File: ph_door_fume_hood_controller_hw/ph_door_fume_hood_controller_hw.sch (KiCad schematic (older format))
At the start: 249 parts, among them IC1 6N137, IC2 6N137, J1 Conn_01x03, J10 Conn_01x03, J11 Conn_01x02, J12 Conn_01x06, J13 Conn_01x02, J14 Conn_01x03, J15 Conn_01x03, J2 Conn_01x04, J3 CONN_01X04, J4 Conn_01x03, J5 Conn_01x03, J6 Conn_01x02, J7 Conn_01x06, J8 USB_OTG, J9 Conn_01x02, M1 DC-DC-24-12V-200mA, M2 MORSUN_485, Q1 C1815, Q10 A1015, Q11 Q_NMOS_GDS, Q2 Q_PMOS_GDS, Q3 Q_NMOS_GDS, Q4 Q_NMOS_GDS, Q5 C1815, Q6 Q_NMOS_GDS, Q7 Q_NMOS_GDS, Q8 C1815, Q9 Q_NMOS_GDS, U1 74HC123, U10 PC817, U11 MCP4725, U12 ASM1117-3V3, U13 PC817, U14 PC817, U15 LM358, U16 PC817, U17 PC817, U18 PC817, U19 PC817, U2 AD8601, U20 PC817, U21 PC817, U22 PC817, U23 PC817, U3 PC817, U4 PC817, U5 TB6600, U6 PC817, U7 STM32F103C8, U8 ASM1117, U9 XL4015, Y1 Crystal, Y2 32768Mhz

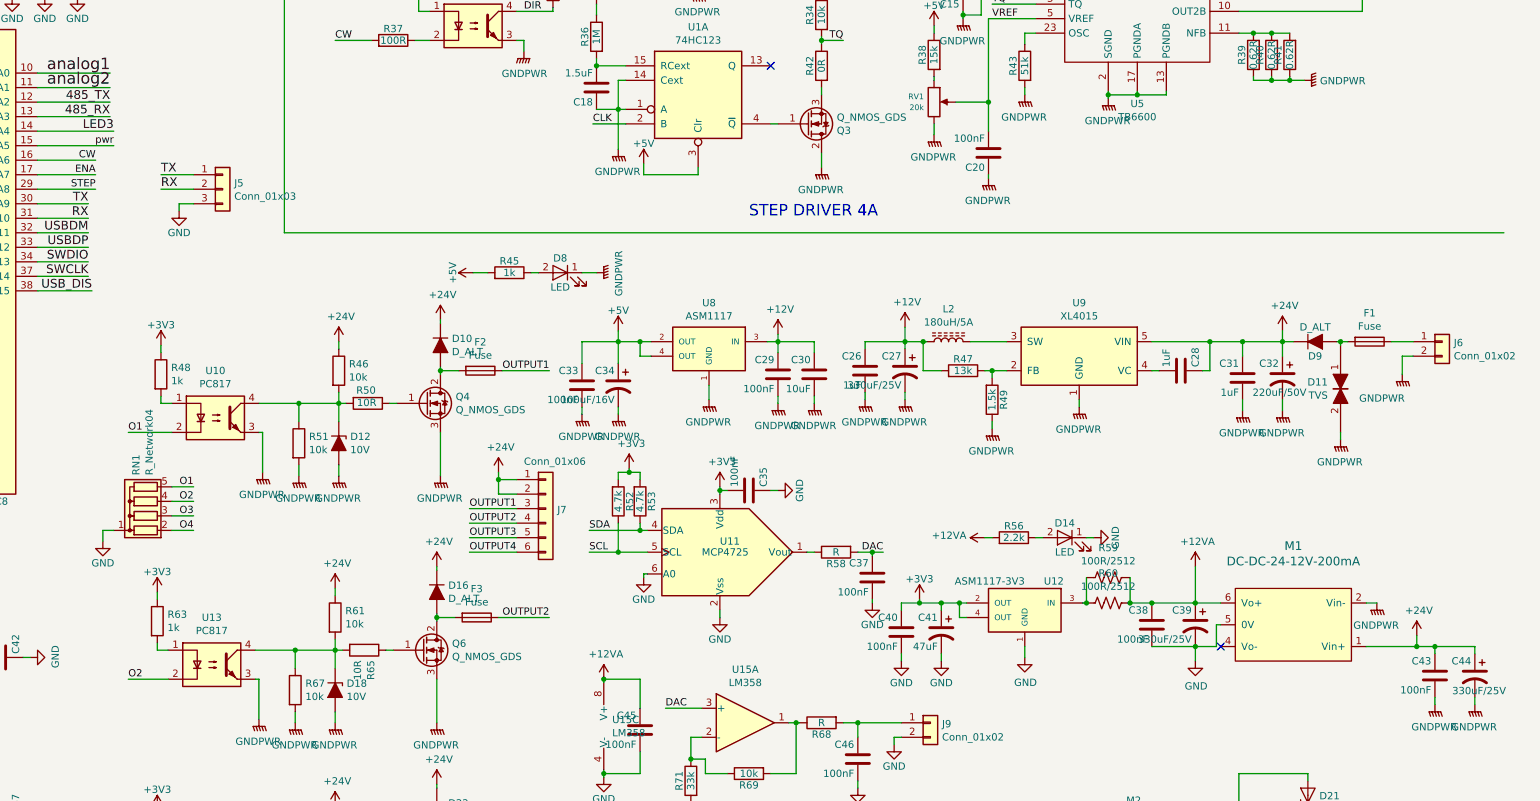
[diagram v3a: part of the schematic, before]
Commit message: door_fume_hood
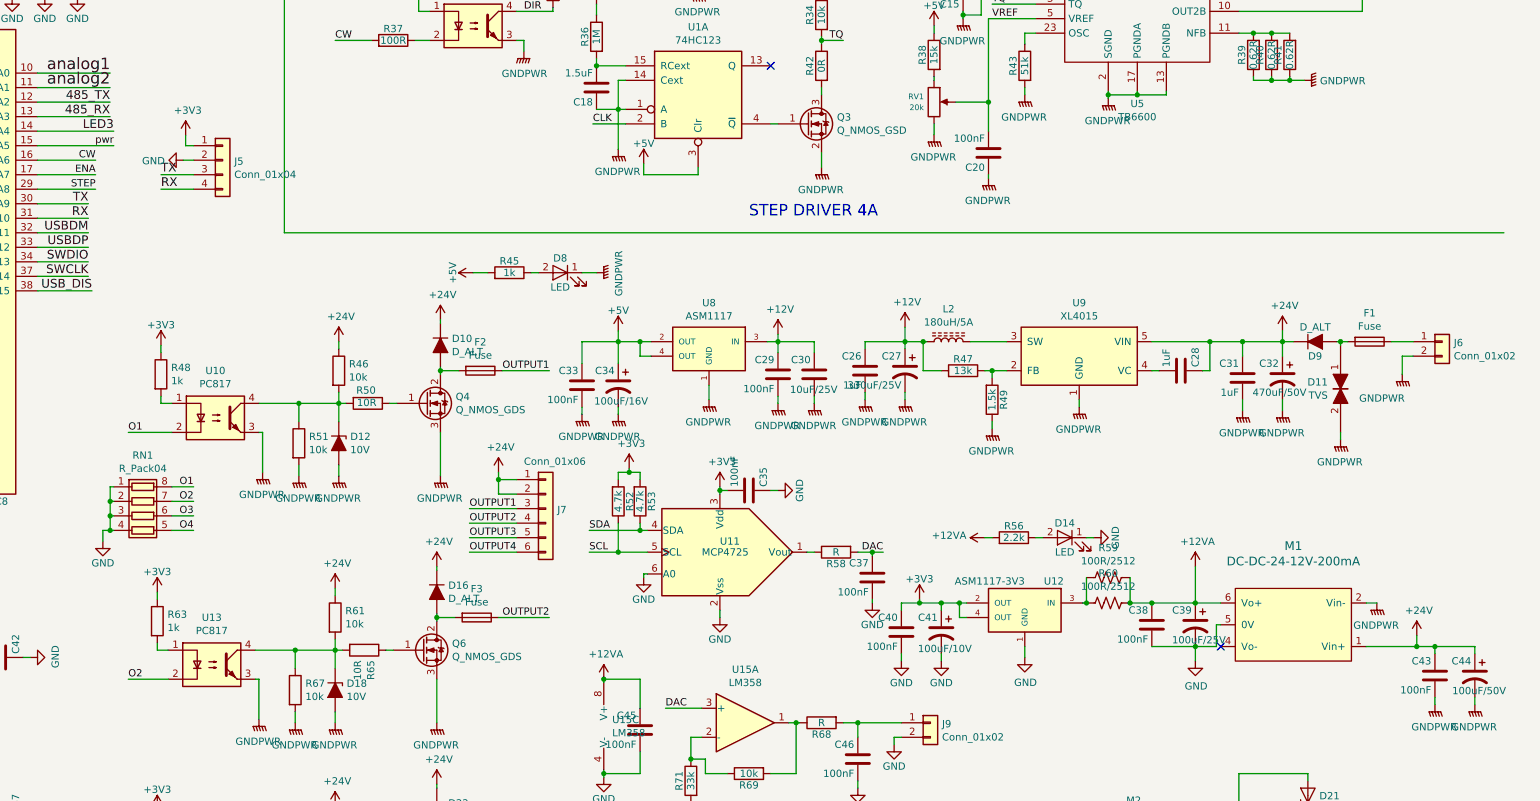
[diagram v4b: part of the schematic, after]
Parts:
- removed J5: Conn_01x03, Connector_PinSocket_2.54mm:PinSocket_1x03_P2.54mm_Vertical, symbol Connector_Generic:Conn_01x03
- removed Q3: Q_NMOS_GDS, VinhTho_Lib:TO-252-2, symbol Device:Q_NMOS_GDS
- removed RN1: R_Network04, Resistor_THT:R_Array_SIP5, symbol Device:R_Network04
- added J5: Conn_01x04, Connector_PinHeader_2.54mm:PinHeader_1x04_P2.54mm_Vertical, symbol Connector_Generic:Conn_01x04
- added Q3: Q_NMOS_GSD, VinhTho_Lib:SOT-23, symbol mcu_water_sample_hw-rescue:Q_NMOS_GSD
- added RN1: R_Pack04, Resistor_SMD:R_Array_Convex_4x0603, symbol Device:R_Pack04
- C27: footprint Capacitor_SMD:C_1210_3225Metric_Pad1.42x2.65mm_HandSolder -> Capacitor_SMD:CP_Elec_8x10.5
- C30: value 10uF -> 10uF/25V; footprint Capacitor_SMD:C_0805_2012Metric_Pad1.15x1.40mm_HandSolder -> Capacitor_SMD:C_1210_3225Metric_Pad1.42x2.65mm_HandSolder
- C32: value 220uF/50V -> 470uF/50V; footprint Capacitor_SMD:C_1210_3225Metric_Pad1.42x2.65mm_HandSolder -> Capacitor_SMD:CP_Elec_10x14.3
- C34: footprint Capacitor_SMD:C_1210_3225Metric_Pad1.42x2.65mm_HandSolder -> Capacitor_SMD:CP_Elec_6.3x5.4
- C39: value 330uF/25V -> 100uF/25V; footprint Capacitor_SMD:C_1210_3225Metric_Pad1.42x2.65mm_HandSolder -> Capacitor_Tantalum_SMD:CP_EIA-7343-20_Kemet-V_Pad2.25x2.55mm_HandSolder
- C41: value 47uF -> 100uF/10V; footprint Capacitor_SMD:C_1210_3225Metric_Pad1.42x2.65mm_HandSolder -> Capacitor_Tantalum_SMD:CP_EIA-3528-15_AVX-H_Pad1.50x2.35mm_HandSolder
- C44: value 330uF/25V -> 100uF/50V; footprint Capacitor_SMD:C_1210_3225Metric_Pad1.42x2.65mm_HandSolder -> Capacitor_Tantalum_SMD:CP_EIA-7343-31_Kemet-D_Pad2.25x2.55mm_HandSolder
- F1: footprint VinhTho_Lib:Fuse_SMD1812 -> VinhTho_Lib:Fuseholder5x20_horiz_SemiClosed_Casing10x25mm
- J11: footprint VinhTho_Lib:TerminalBlock_WAGO-236_2Stift_R5mm_2pol -> VinhTho_Lib:TerminalBlock_WAGO_2.54mm_2P
- J12: footprint VinhTho_Lib:TerminalBlock-WAGO-6P -> VinhTho_Lib:TerminalBlock_WAGO_2.54mm_6P
- J2: footprint VinhTho_Lib:Domino-5.08mm_4pol -> VinhTho_Lib:TerminalBlock_WAGO-236_2Stift_R5mm_4pol
- L2: footprint VinhTho_Lib:L181-5A -> VinhTho_Lib:Inductor_5A
- RV1: footprint VinhTho_Lib:VR1 -> VinhTho_Lib:VR-3362P
- U10, U13, U14, U16, U17, U18, U19, U20, U21, U22, U23, U3, U4, U6: footprint Package_DIP:DIP-4_W7.62mm -> VinhTho_Lib:Optocoupler_SMD
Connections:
- net +3V3: now also J5.1 (Pin_1)
- net GND: now also J5.2 (Pin_2), RN1.1 (R1.1), RN1.2 (R2.1), RN1.3 (R3.1), RN1.4 (R4.1)
- net GNDPWR: now also Q3.2 (S)
- net O1: now also RN1.8 (R1.2)
- net O2: now also RN1.7 (R2.2)
- net O3: now also RN1.6 (R3.2)
- net O4: now also RN1.5 (R4.2)
- net RX: now also J5.4 (Pin_4)
- net TX: now also J5.3 (Pin_3)
- net at U1.4 (~Q): now also Q3.1 (G)
- net at R42.2: now also Q3.3 (D)

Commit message: Layoutting door fume
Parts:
- removed Q11, Q4, Q6, Q7, Q9: Q_NMOS_GDS, VinhTho_Lib:TO-252-2, symbol Device:Q_NMOS_GDS
- removed R25, R5: 0R, Resistor_SMD:R_0805_2012Metric_Pad1.15x1.40mm_HandSolder, symbol Device:R
- added Q11, Q4, Q6, Q7, Q9: Q_NMOS_GSD, VinhTho_Lib:SOT-23, symbol Device:Q_NMOS_GSD
- J13: footprint VinhTho_Lib:TerminalBlock_WAGO-236_2Stift_R5mm_2pol -> VinhTho_Lib:TerminalBlock_WAGO_2.54mm_2P
- J7: footprint VinhTho_Lib:TerminalBlock-WAGO-6P -> VinhTho_Lib:TerminalBlock_WAGO_2.54mm_6P
- J9: footprint VinhTho_Lib:TerminalBlock_WAGO-236_2Stift_R5mm_2pol -> Connector_PinSocket_2.54mm:PinSocket_1x02_P2.54mm_Vertical
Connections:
- net +3V3: now also D15.1 (K), LS1.1
- net +5V: no longer C36.1, D13.1 (K), D15.1 (K), LS1.1
- net GNDPWR: now also Q11.2 (S), Q4.2 (S), Q6.2 (S), Q7.2 (S), Q9.2 (S)
- net at R50.1: now also Q4.1 (G)
- net at D10.2 (A), F2.2: now also Q4.3 (D)
- net at R65.1: now also Q6.1 (G)
- net at D16.2 (A), F3.2: now also Q6.3 (D)
- net at R77.1: now also Q7.1 (G)
- net at D22.2 (A), F4.2: now also Q7.3 (D)
- net at R93.1: now also Q11.1 (G)
- net at D30.2 (A), F7.2: now also Q11.3 (D)
- net at R87.1: now also Q9.1 (G)
- net at D26.2 (A), J13.2 (Pin_2): now also Q9.3 (D)
- new net +5VA: C36.1, D13.1 (K)
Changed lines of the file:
@@
 $EndComp
 $Comp
-L master-node-rescue:+5V #PWR0108
-U 1 1 5A52FEE6
-P 1700 5875
-F 0 "#PWR0108" H 1700 5725 50  0001 C CNN
-F 1 "+5V" H 1700 6015 50  0000 C CNN
-F 2 "" H 1700 5875 50  0001 C CNN
-F 3 "" H 1700 5875 50  0001 C CNN
-	1    1700 5875
-	1    0    0    -1
-$EndComp
-$Comp
-L master-node-rescue:D_ALT D13
-U 1 1 5A531888
-P 1450 5925
-F 0 "D13" H 1450 6025 50  0000 C CNN
-F 1 "D_ALT" H 1450 5825 50  0000 C CNN
-F 2 "VinhTho_Lib:D_SOD-323F" H 1450 5925 50  0001 C CNN
-F 3 "" H 1450 5925 50  0001 C CNN
-	1    1450 5925
-	-1   0    0    1
-$EndComp
-$Comp
 L master-node-rescue:R R55
 U 1 1 5A533DDA
@@
 $EndComp
 $Comp
-L master-node-rescue:+5V #PWR0116
-U 1 1 5A549BE9
-P 525 6050
-F 0 "#PWR0116" H 525 5900 50  0001 C CNN
-F 1 "+5V" H 525 6190 50  0000 C CNN
-F 2 "" H 525 6050 50  0001 C CNN
-F 3 "" H 525 6050 50  0001 C CNN
-	1    525  6050
-	1    0    0    -1
-$EndComp
-$Comp
 L master-node-rescue:CONN_01X04 J3
 U 1 1 5A54E099
@@
 	2950 5025 2600 5025
 Wire Wire Line
-	1300 5925 1300 6125
-Wire Wire Line
 	1300 6325 1350 6325
 Wire Wire Line
@@
 	2525 6600 2700 6600
 $Comp
-L master-node-rescue:+5V #PWR0121
-U 1 1 5F75627A
-P 2750 6375
-F 0 "#PWR0121" H 2750 6225 50  0001 C CNN
-F 1 "+5V" H 2750 6515 50  0000 C CNN
-F 2 "" H 2750 6375 50  0001 C CNN
-F 3 "" H 2750 6375 50  0001 C CNN
-	1    2750 6375
-	1    0    0    -1
-$EndComp
-Wire Wire Line
-	2750 6375 2750 6425
-$Comp
 L ph_door_fume_hood_controller_hw-rescue:C1815-nhantt-kicad-lib Q5
 U 1 1 5F78DF98
@@
 	1    0    0    -1
 $EndComp
-Wire Wire Line
-	1400 1725 1400 1700
 $Comp
 L power:GND #PWR034
@@
 in4
 $Comp
-L Device:R R25
-U 1 1 5DBE6FC7
-P 1125 1700
-F 0 "R25" H 1195 1746 50  0000 L CNN
-F 1 "0R" H 1195 1655 50  0000 L CNN
-F 2 "Resistor_SMD:R_0805_2012Metric_Pad1.15x1.40mm_HandSolder" V 1055 1700 50  0001 C CNN
-F 3 "~" H 1125 1700 50  0001 C CNN
-	1    1125 1700
-	0    1    1    0
-$EndComp
-Wire Wire Line
-	1275 1700 1400 1700
-Connection ~ 1400 1700
-Wire Wire Line
-	1400 1700 1400 1650
-$Comp
-L power:GNDPWR #PWR035
-U 1 1 5DC90838
-P 875 1750
-F 0 "#PWR035" H 875 1550 50  0001 C CNN
-F 1 "GNDPWR" H 880 1596 50  0000 C CNN
-F 2 "" H 875 1700 50  0001 C CNN
-F 3 "" H 875 1700 50  0001 C CNN
-	1    875  1750
-	-1   0    0    -1
-$EndComp
-Wire Wire Line
-	875  1750 875  1700
-Wire Wire Line
-	875  1700 975  1700
-$Comp
 L Device:R R4
 U 1 1 5DD3B3C6
@@
 	-1   0    0    1
 $EndComp
-$Comp
-L Device:R R5
-U 1 1 5DD3B78D
-P 1375 900
-F 0 "R5" H 1445 946 50  0000 L CNN
-F 1 "0R" H 1445 855 50  0000 L CNN
-F 2 "Resistor_SMD:R_0805_2012Metric_Pad1.15x1.40mm_HandSolder" V 1305 900 50  0001 C CNN
-F 3 "~" H 1375 900 50  0001 C CNN
-	1    1375 900
-	-1   0    0    1
-$EndComp
-Wire Wire Line
-	1100 1050 1375 1050
 Wire Wire Line
 	975  1050 1100 1050
-Connection ~ 1100 1050
 Wire Wire Line
 	1100 700  1100 750
@@
 	2125 2675 2075 2675
 $Comp
-L Device:Q_NMOS_GDS Q4
-U 1 1 5E6FB3F9
-P 8625 5400
-F 0 "Q4" H 8830 5446 50  0000 L CNN
-F 1 "Q_NMOS_GDS" H 8830 5355 50  0000 L CNN
-F 2 "VinhTho_Lib:TO-252-2" H 8825 5500 50  0001 C CNN
-F 3 "https://banlinhkien.com/30n06-fqd30n06-to252-mosfet-nch-22a-60v-p12118703.html" H 8625 5400 50  0001 C CNN
-	1    8625 5400
-	1    0    0    -1
-$EndComp
-$Comp
 L Device:R R50
 U 1 1 5E6FB731
@@
 	6800 5000 6800 5050
 $Comp
-L Device:Q_NMOS_GDS Q6
-U 1 1 5EF4FCDE
-P 8600 7100
-F 0 "Q6" H 8805 7146 50  0000 L CNN
-F 1 "Q_NMOS_GDS" H 8805 7055 50  0000 L CNN
-F 2 "VinhTho_Lib:TO-252-2" H 8800 7200 50  0001 C CNN
-F 3 "https://banlinhkien.com/30n06-fqd30n06-to252-mosfet-nch-22a-60v-p12118703.html" H 8600 7100 50  0001 C CNN
-	1    8600 7100
-	1    0    0    -1
-$EndComp
-$Comp
 L Device:R R65
 U 1 1 5EF4FCE4
@@
 $EndComp
 $Comp
-L Device:Q_NMOS_GDS Q7
-U 1 1 5F2858BF
-P 8600 8600
-F 0 "Q7" H 8805 8646 50  0000 L CNN
-F 1 "Q_NMOS_GDS" H 8805 8555 50  0000 L CNN
-F 2 "VinhTho_Lib:TO-252-2" H 8800 8700 50  0001 C CNN
-F 3 "https://banlinhkien.com/30n06-fqd30n06-to252-mosfet-nch-22a-60v-p12118703.html" H 8600 8600 50  0001 C CNN
-	1    8600 8600
-	1    0    0    -1
-$EndComp
-$Comp
 L Device:R R77
 U 1 1 5F2858C5
@@
 	6775 8200 6775 8250
 $Comp
-L Device:Q_NMOS_GDS Q11
-U 1 1 5F285936
-P 8575 10300
-F 0 "Q11" H 8780 10346 50  0000 L CNN
-F 1 "Q_NMOS_GDS" H 8780 10255 50  0000 L CNN
-F 2 "VinhTho_Lib:TO-252-2" H 8775 10400 50  0001 C CNN
-F 3 "https://banlinhkien.com/30n06-fqd30n06-to252-mosfet-nch-22a-60v-p12118703.html" H 8575 10300 50  0001 C CNN
-	1    8575 10300
-	1    0    0    -1
-$EndComp
-$Comp
 L Device:R R93
 U 1 1 5F28593C
@@
 $EndComp
 $Comp
-L Device:Q_NMOS_GDS Q9
-U 1 1 610BF886
-P 11975 9450
-F 0 "Q9" H 12180 9496 50  0000 L CNN
-F 1 "Q_NMOS_GDS" H 12180 9405 50  0000 L CNN
-F 2 "VinhTho_Lib:TO-252-2" H 12175 9550 50  0001 C CNN
-F 3 "https://banlinhkien.com/30n06-fqd30n06-to252-mosfet-nch-22a-60v-p12118703.html" H 11975 9450 50  0001 C CNN
-	1    11975 9450
-	1    0    0    -1
-$EndComp
-$Comp
 L power:GNDPWR #PWR0188
 U 1 1 611442E5
@@
 F 0 "J13" H 12630 9117 50  0000 L CNN
 F 1 "Conn_01x02" H 12630 9026 50  0000 L CNN
-F 2 "VinhTho_Lib:TerminalBlock_WAGO-236_2Stift_R5mm_2pol" H 12550 9125 50  0001 C CNN
+F 2 "VinhTho_Lib:TerminalBlock_WAGO_2.54mm_2P" H 12550 9125 50  0001 C CNN
 F 3 "~" H 12550 9125 50  0001 C CNN
 	1    12550 9125
@@
 	1    0    0    -1
 $EndComp
-Wire Wire Line
-	1375 700  1375 750
 $Comp
 L Device:R_US R60
@@
 F 0 "J9" H 12180 7592 50  0000 L CNN
 F 1 "Conn_01x02" H 12180 7501 50  0000 L CNN
-F 2 "VinhTho_Lib:TerminalBlock_WAGO-236_2Stift_R5mm_2pol" H 12100 7600 50  0001 C CNN
+F 2 "Connector_PinSocket_2.54mm:PinSocket_1x02_P2.54mm_Vertical" H 12100 7600 50  0001 C CNN
 F 3 "~" H 12100 7600 50  0001 C CNN
 	1    12100 7600
@@
 F 0 "J7" H 9530 6117 50  0000 L CNN
 F 1 "Conn_01x06" H 9300 6450 50  0000 L CNN
-F 2 "VinhTho_Lib:TerminalBlock-WAGO-6P" H 9450 6125 50  0001 C CNN
+F 2 "VinhTho_Lib:TerminalBlock_WAGO_2.54mm_6P" H 9450 6125 50  0001 C CNN
 F 3 "~" H 9450 6125 50  0001 C CNN
 	1    9450 6125
@@
 $EndComp
 $Comp
-L power:+24V #PWR0213
-U 1 1 5DC75FC2
-P 1375 700
-F 0 "#PWR0213" H 1375 550 50  0001 C CNN
-F 1 "+24V" H 1390 873 50  0000 C CNN
-F 2 "" H 1375 700 50  0001 C CNN
-F 3 "" H 1375 700 50  0001 C CNN
-	1    1375 700
-	1    0    0    -1
-$EndComp
-$Comp
 L master-node-rescue:C C10
 U 1 1 595ADDFC
@@
 Wire Wire Line
 	6955 3725 7025 3725
+$Comp
+L Device:Q_NMOS_GSD Q4
+U 1 1 5DCB7A9F
+P 8625 5400
+F 0 "Q4" H 8831 5446 50  0000 L CNN
+F 1 "Q_NMOS_GSD" H 8831 5355 50  0000 L CNN
+F 2 "VinhTho_Lib:SOT-23" H 8825 5500 50  0001 C CNN
+F 3 "~" H 8625 5400 50  0001 C CNN
+	1    8625 5400
+	1    0    0    -1
+$EndComp
+$Comp
+L Device:Q_NMOS_GSD Q6
+U 1 1 5DCD479A
+P 8600 7100
+F 0 "Q6" H 8806 7146 50  0000 L CNN
+F 1 "Q_NMOS_GSD" H 8806 7055 50  0000 L CNN
+F 2 "VinhTho_Lib:SOT-23" H 8800 7200 50  0001 C CNN
+F 3 "~" H 8600 7100 50  0001 C CNN
+	1    8600 7100
+	1    0    0    -1
+$EndComp
+$Comp
+L Device:Q_NMOS_GSD Q7
+U 1 1 5DCE889D
+P 8600 8600
+F 0 "Q7" H 8806 8646 50  0000 L CNN
+F 1 "Q_NMOS_GSD" H 8806 8555 50  0000 L CNN
+F 2 "VinhTho_Lib:SOT-23" H 8800 8700 50  0001 C CNN
+F 3 "~" H 8600 8600 50  0001 C CNN
+	1    8600 8600
+	1    0    0    -1
+$EndComp
+$Comp
+L Device:Q_NMOS_GSD Q11
+U 1 1 5DCEFDC2
+P 8575 10300
+F 0 "Q11" H 8781 10346 50  0000 L CNN
+F 1 "Q_NMOS_GSD" H 8781 10255 50  0000 L CNN
+F 2 "VinhTho_Lib:SOT-23" H 8775 10400 50  0001 C CNN
+F 3 "~" H 8575 10300 50  0001 C CNN
+	1    8575 10300
+	1    0    0    -1
+$EndComp
+$Comp
+L Device:Q_NMOS_GSD Q9
+U 1 1 5DCFDDF3
+P 11975 9450
+F 0 "Q9" H 12181 9496 50  0000 L CNN
+F 1 "Q_NMOS_GSD" H 12181 9405 50  0000 L CNN
+F 2 "VinhTho_Lib:SOT-23" H 12175 9550 50  0001 C CNN
+F 3 "~" H 11975 9450 50  0001 C CNN
+	1    11975 9450
+	1    0    0    -1
+$EndComp
+Wire Wire Line
+	1400 1650 1400 1725
+$Comp
+L master-node-rescue:+3V3 #PWR0108
+U 1 1 5E2D6D01
+P 2750 6375
+F 0 "#PWR0108" H 2750 6225 50  0001 C CNN
+F 1 "+3V3" H 2750 6515 50  0000 C CNN
+F 2 "" H 2750 6375 50  0001 C CNN
+F 3 "" H 2750 6375 50  0001 C CNN
+	1    2750 6375
+	1    0    0    -1
+$EndComp
+Wire Wire Line
+	1300 5925 1300 6125
+$Comp
+L master-node-rescue:D_ALT D13
+U 1 1 5A531888
+P 1450 5925
+F 0 "D13" H 1450 6025 50  0000 C CNN
+F 1 "D_ALT" H 1450 5825 50  0000 C CNN
+F 2 "VinhTho_Lib:D_SOD-323F" H 1450 5925 50  0001 C CNN
+F 3 "" H 1450 5925 50  0001 C CNN
+	1    1450 5925
+	-1   0    0    1
+$EndComp
+$Comp
+L power:+5VA #PWR0121
+U 1 1 5E3810D0
+P 1700 5875
+F 0 "#PWR0121" H 1700 5725 50  0001 C CNN
+F 1 "+5VA" H 1715 6048 50  0000 C CNN
+F 2 "" H 1700 5875 50  0001 C CNN
+F 3 "" H 1700 5875 50  0001 C CNN
+	1    1700 5875
+	1    0    0    -1
+$EndComp
+Wire Wire Line
+	2750 6375 2750 6425
+$Comp
+L power:+5VA #PWR?
+U 1 1 5DEAC768
+P 525 6050
+F 0 "#PWR?" H 525 5900 50  0001 C CNN
+F 1 "+5VA" H 540 6223 50  0000 C CNN
+F 2 "" H 525 6050 50  0001 C CNN
+F 3 "" H 525 6050 50  0001 C CNN
+	1    525  6050
+	1    0    0    -1
+$EndComp
 $EndSCHEMATC
